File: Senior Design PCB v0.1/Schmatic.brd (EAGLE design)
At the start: 204.4 x 100 mm, 213 parts, among them IC1 TMC2208, IC2 TMC2208, IC3 TMC2208, IC4 TMC2208, IC5 TMC2208, IC6 CP2104, J1 XT60PW-M, J3 XT60PW-M, Q1 mmbt2222, Q2 mmbt2222, Q3 MMBT4403, Q4 AOD417, Q5 MMBT4403, Q6 MMBT4403, Q7 DMG3415U, U1 PCA9685, U2 AP2112-3.3, U3 HTU21DF, U4 HX711, U5 HX711, U6 HX711, X2 ESP32_WROOM32_SKINNY

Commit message: done layout, waiting for signal wire pin config
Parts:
- removed FAN, VIBRATION: S2B-PH-SM4_TB, NewKevinMade:S2B-PH-SM4_TB
- removed J1, J3: XT60PW-M, XT60PW-M:AMASS_XT60PW-M
- added 12V_IN, 5V_IN: XT60PW-M, XT60PW-M:AMASS_XT60PW-M
- added C67, C69, C70, C71, C72, C73: 100uF, SparkFun-Capacitors:PANASONIC_D
- added C68: 560uF, SparkFun-Capacitors:PANASONIC_G
- added D7, D8: RED, microbuilder:CHIPLED_0805_NOOUTLINE
- added FAN_, VIBRATION_: B2B-PH-SM4-TB(LF)(SN), B2B-PH-SM4-TB_LF__SN_:JST_B2B-PH-SM4-TB(LF)(SN)
- added R70, R86: 1K, microbuilder:0603-NO@1
- added STEPPER1, STEPPER2, STEPPER3, STEPPER4, STEPPER5: S4B-PH-SM4_TB, NewKevinMade:S4B-PH-SM4_TB
- added U$48, U$49, U$50: MOUNTINGHOLE2.5, microbuilder:MOUNTINGHOLE_2.5_PLATED
- added WEIGHT_SENSOR: S5B-PH-SM4_TB, NewKevinMade:S5B-PH-SM4_TB
- C3: value (none) -> 560uF; device adafruit:E3,5-8 -> SparkFun-Capacitors:PANASONIC_G
- C66: value 560uF -> 100uF; device SparkFun-Capacitors:PANASONIC_G -> SparkFun-Capacitors:PANASONIC_D
- LIQUID_RELEASE_SW, SOLID_RELEASE_SW, X-HOMING-SW, Y-HOMING-SW: value S2B-PH-SM4_TB -> B2B-PH-SM4-TB(LF)(SN); device NewKevinMade:S2B-PH-SM4_TB -> B2B-PH-SM4-TB_LF__SN_:JST_B2B-PH-SM4-TB(LF)(SN)
- ROTARY_SWITCH: value S5B-PH-SM4_TB -> B5B-PH-SM4-TB; device NewKevinMade:S5B-PH-SM4_TB -> B2B-PH-SM4-TB_LF__SN_:JST_B5B-PH-SM4-TB
- U$4: value S5B-PH-SM4_TB -> MOUNTINGHOLE2.5; device NewKevinMade:S5B-PH-SM4_TB -> microbuilder:MOUNTINGHOLE_2.5_PLATED
- moved U$9 563.1 mm to (25.4, 63.5), turned to 180 degrees
- moved LIQUID_LATCH 539.7 mm to (73.7, 24.1), flipped to the bottom
- moved SOLID_LATCH 521.9 mm to (55.9, 24.1), flipped to the bottom
- moved R83 512.9 mm to (69.8, 35.6), flipped to the bottom, turned to 90 degrees
- moved R84 507.6 mm to (52.1, 35.6), flipped to the bottom, turned to 90 degrees
- moved CATCHER_LATCH 504.3 mm to (38.1, 24.1), flipped to the bottom
- moved R85 501.3 mm to (39.4, 31.8), flipped to the bottom, turned to 270 degrees
- moved R82 500.5 mm to (11.4, 49.5), flipped to the bottom, turned to 270 degrees
- moved R81 487.4 mm to (11.4, 38.1), flipped to the bottom, turned to 270 degrees
- moved R71 481.7 mm to (80.0, 25.4), flipped to the bottom, turned to 90 degrees
- moved R72 472.9 mm to (80.0, 12.7), flipped to the bottom, turned to 90 degrees
- moved R73 472.7 mm to (77.5, 11.4), flipped to the bottom, turned to 90 degrees
- moved R74 469.4 mm to (66.0, 11.4), flipped to the bottom, turned to 90 degrees
- moved R69 468.9 mm to (71.1, 39.4), turned to 90 degrees
- moved R75 466.3 mm to (54.6, 11.4), flipped to the bottom, turned to 90 degrees
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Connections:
- removed net N$29: X-HOMING-SW.1
- removed net N$30: X-HOMING-SW.2
- removed net N$31: Y-HOMING-SW.1
- removed net N$32: Y-HOMING-SW.2
- new net N$53: D7.A, R70.2
- new net N$55: D8.A, R86.2
- new net X-HOMING: R70.1, X-HOMING-SW.2
- new net Y-HOMING: R86.1, Y-HOMING-SW.2
- net 12V_REG: now also 12V_IN.1, C69.+, C70.+, C71.+, C72.+, C73.+; no longer J1.1
- net 5V_REG: now also 5V_IN.1, FAN_.2, VIBRATION_.2; no longer FAN.2, J3.1, VIBRATION.2
- net 5V_SERVO: now also C68.+
- net A+_2: now also WEIGHT_SENSOR.4; no longer U$4.4
- net A-_2: now also WEIGHT_SENSOR.3; no longer U$4.3
- net AVDD_2: now also WEIGHT_SENSOR.1; no longer U$4.1
- net FAN_5V: now also FAN_.1; no longer FAN.1
- net GND: now also 12V_IN.2, 5V_IN.2, C67.-, C68.-, C69.-, C70.-, C71.-, C72.-, C73.-, D7.C, D8.C, ROTARY_SWITCH.6, WEIGHT_SENSOR.2, WEIGHT_SENSOR.5; no longer J1.2, J3.2, ROTARY_SWITCH.4, U$4.2, U$4.5
- net OA1_1: now also STEPPER1.1
- net OA1_2: now also STEPPER2.1
- net OA1_3: now also STEPPER3.1
- net OA1_4: now also STEPPER4.1
- net OA1_5: now also STEPPER5.1
- net OA2_1: now also STEPPER1.2
- net OA2_2: now also STEPPER2.2
- net OA2_3: now also STEPPER3.2
- net OA2_4: now also STEPPER4.2
- net OA2_5: now also STEPPER5.2
- net OB1_1: now also STEPPER1.3
- net OB1_2: now also STEPPER2.3
- net OB1_3: now also STEPPER3.3
- net OB1_4: now also STEPPER4.3
- net OB1_5: now also STEPPER5.3
- net OB2_1: now also STEPPER1.4
- net OB2_2: now also STEPPER2.4
- net OB2_3: now also STEPPER3.4
- net OB2_4: now also STEPPER4.4
- net OB2_5: now also STEPPER5.4
- net ROTA_C: now also ROTARY_SWITCH.5; no longer ROTARY_SWITCH.3
- net ROTA_E: now also ROTARY_SWITCH.7; no longer ROTARY_SWITCH.5
- net VCC: now also C67.+, X-HOMING-SW.1, Y-HOMING-SW.1
- net VIB_5V: now also VIBRATION_.1; no longer VIBRATION.1
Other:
- board size 204.4 x 100 mm -> 90.2 x 65.7 mm

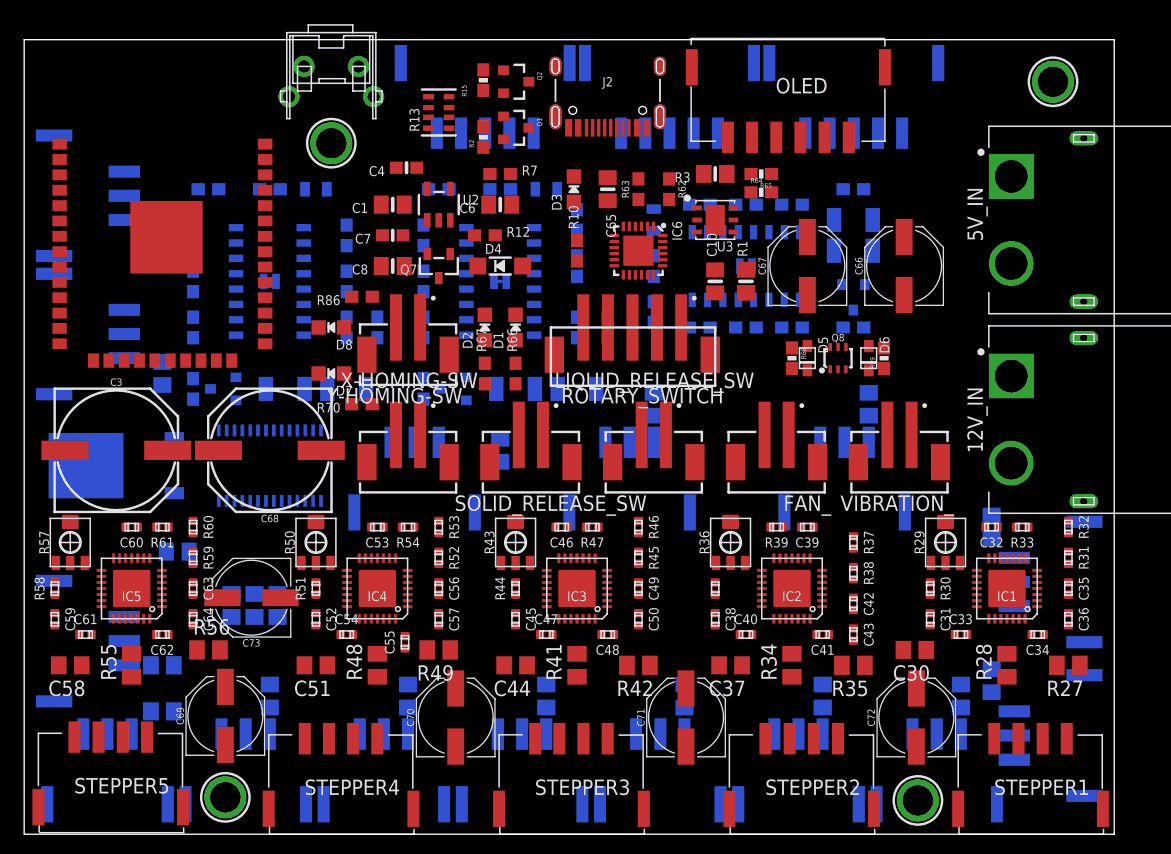
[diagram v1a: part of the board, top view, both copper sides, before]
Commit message: update pcb layout, finishedd net class assignment. assigned gnd plane, signal plane and Vref plane
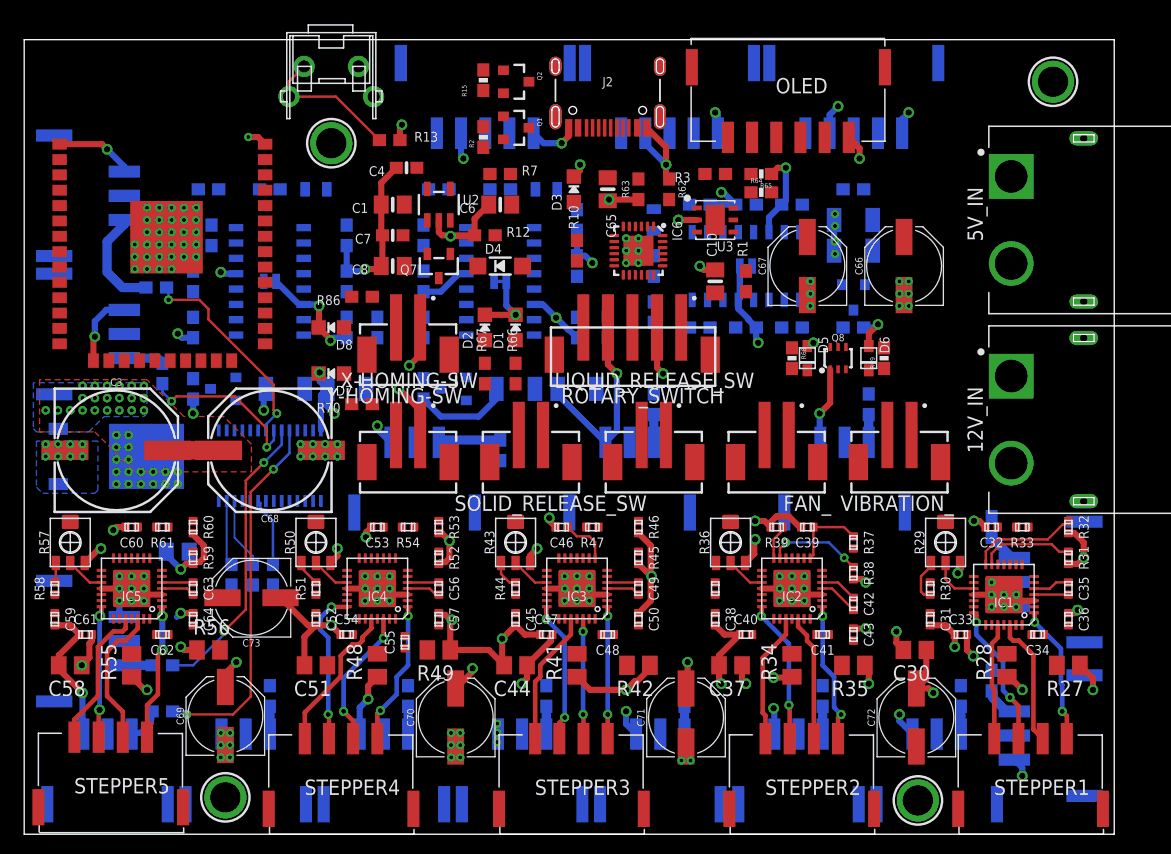
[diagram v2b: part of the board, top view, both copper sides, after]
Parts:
- R1, R3, R4, R6, R8: value 10K -> 10k; device microbuilder:0805-NO@1 -> SparkFun-Resistors:0603
- R13: value 10K -> 10k; device microbuilder:RESPACK_4X0603 -> SparkFun-Resistors:0603
- R71, R72, R73, R74, R75, R76, R77, R78, R79, R80, R81, R82, R83, R84, R85: value 220 -> 22; device microbuilder:0805-NO@1 -> SparkFun-Resistors:0603
- moved R13 4.66 mm to (30.2, 57.4), turned to 0 degrees
- moved R6 4.58 mm to (17.1, 21.5)
- moved R82 4.35 mm to (10.9, 45.2), turned to 180 degrees
- moved R8 3.10 mm to (18.9, 21.5)
- moved R4 2.96 mm to (20.6, 21.5)
- moved C25 1.52 mm to (15.5, 49.5)
- moved Q4 0.76 mm to (7.62, 31.2), turned to 90 degrees
- moved IC1 0.57 mm to (81.0, 19.8)
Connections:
- net N$54: now also R13.1; no longer R13.6
- net VCC: now also R13.2; no longer R13.3
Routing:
- net GND: track 0.00 -> 321.4 mm, vias 0 -> 199
- net N$46: track 0.00 -> 30.5 mm, vias 0 -> 2
- net N$47: track 0.00 -> 24.2 mm, vias 0 -> 2
- net 12V_REG: track 0.00 -> 23.6 mm, vias 0 -> 8
- net N$49: track 0.00 -> 17.5 mm, vias 0 -> 2
- net N$48: track 0.00 -> 14.1 mm, vias 0 -> 2
- net OA2_4: track 0.00 -> 12.9 mm, vias 0 -> 2
- net OA1_4: track 0.00 -> 12.5 mm
- net OA1_5: track 0.00 -> 12.0 mm
- net N$54: track 0.00 -> 12.0 mm
- net OA2_1: track 0.00 -> 11.9 mm, vias 0 -> 2
- net OB2_4: track 0.00 -> 11.9 mm, vias 0 -> 2
- net OA2_2: track 0.00 -> 11.9 mm, vias 0 -> 2
- net OB1_5: track 0.00 -> 11.7 mm
- net OA2_3: track 0.00 -> 11.7 mm, vias 0 -> 2
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- added copper zone on layer 15, net 12V_REG
- added copper zone on layer 15, net 5V_REG
- added copper zone on layer 1, net 5V_SERVO
- added copper zone on layer 16, net 5V_SERVO
- added copper zone on layer 16, net GND
- added copper zone on layer 2, net GND
- added copper zone on layer 15, net VCC
